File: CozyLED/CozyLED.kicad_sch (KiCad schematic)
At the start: 31 parts, among them J1 BOOT, J3 UART, J4 JTAG, J5 RGB OUT, J6 USB_C_Receptacle_PowerOnly_6P, Q1 Q_NMOS_GDS, Q2 Q_NMOS_GDS, Q3 Q_NMOS_GDS, SW1 SW_Push, U2 LMR16006YQ3, Y1 32.768kHz

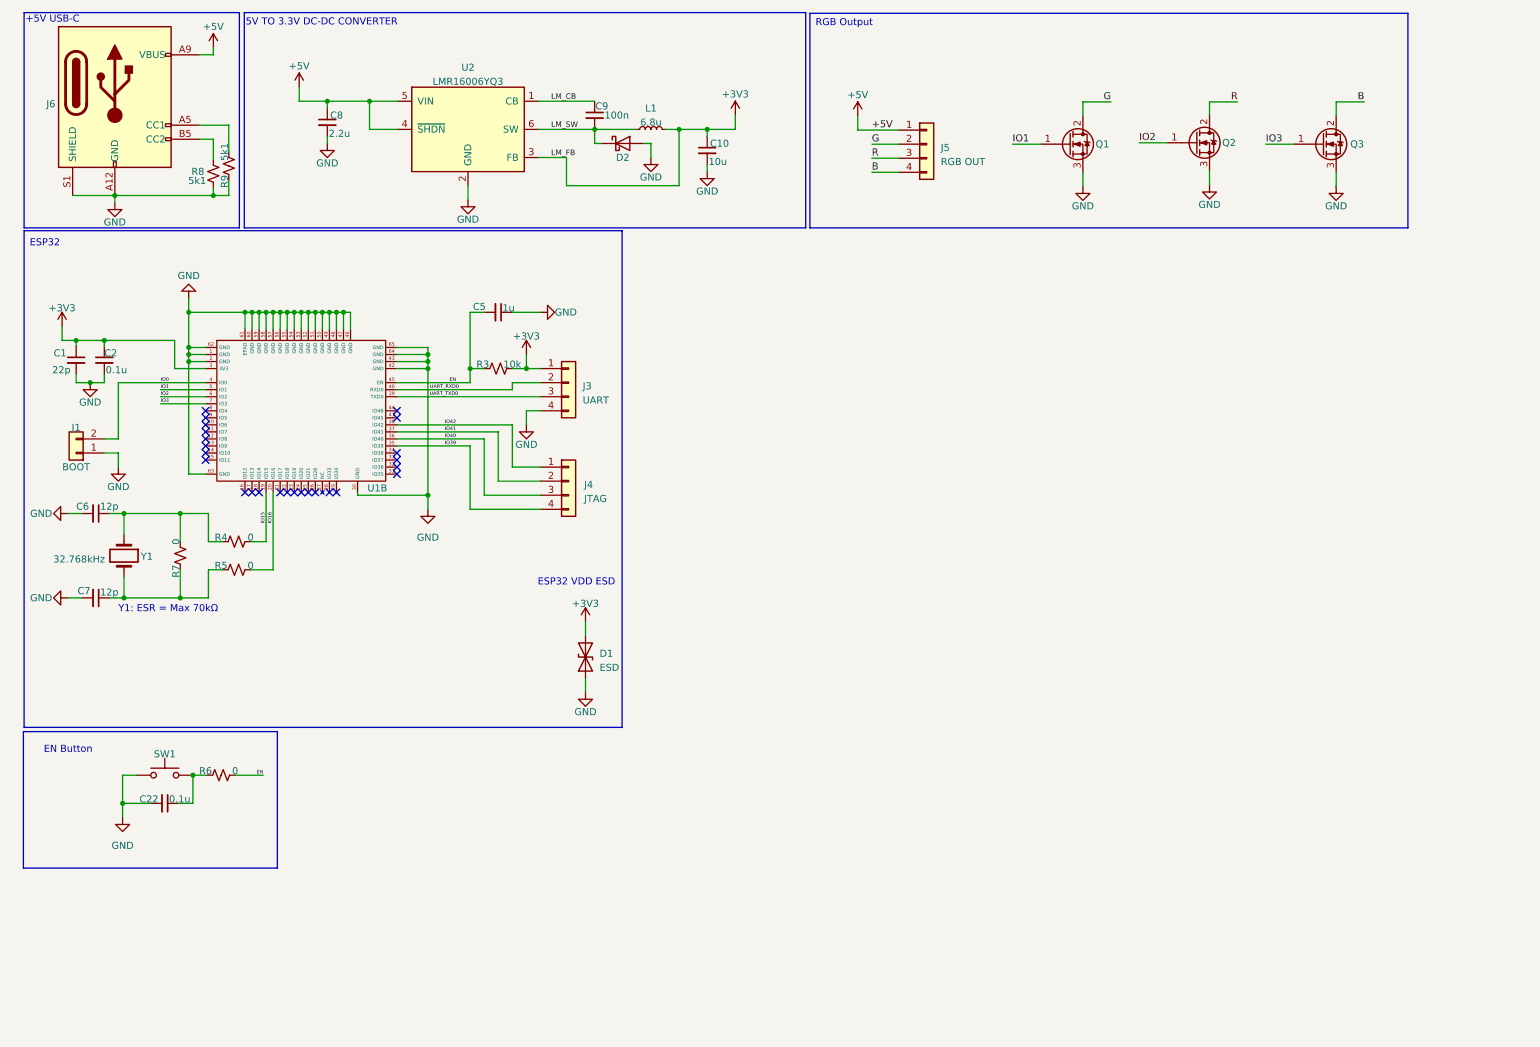
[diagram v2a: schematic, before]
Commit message: Updated Code v0.1
Updates
- Added code for LCD drawings of mode label and triangles to depict button presses (still need actual press drawing)
- Added initial code for mode transition by button hold (2.5 seconds for now)
- Cleaned up some test code
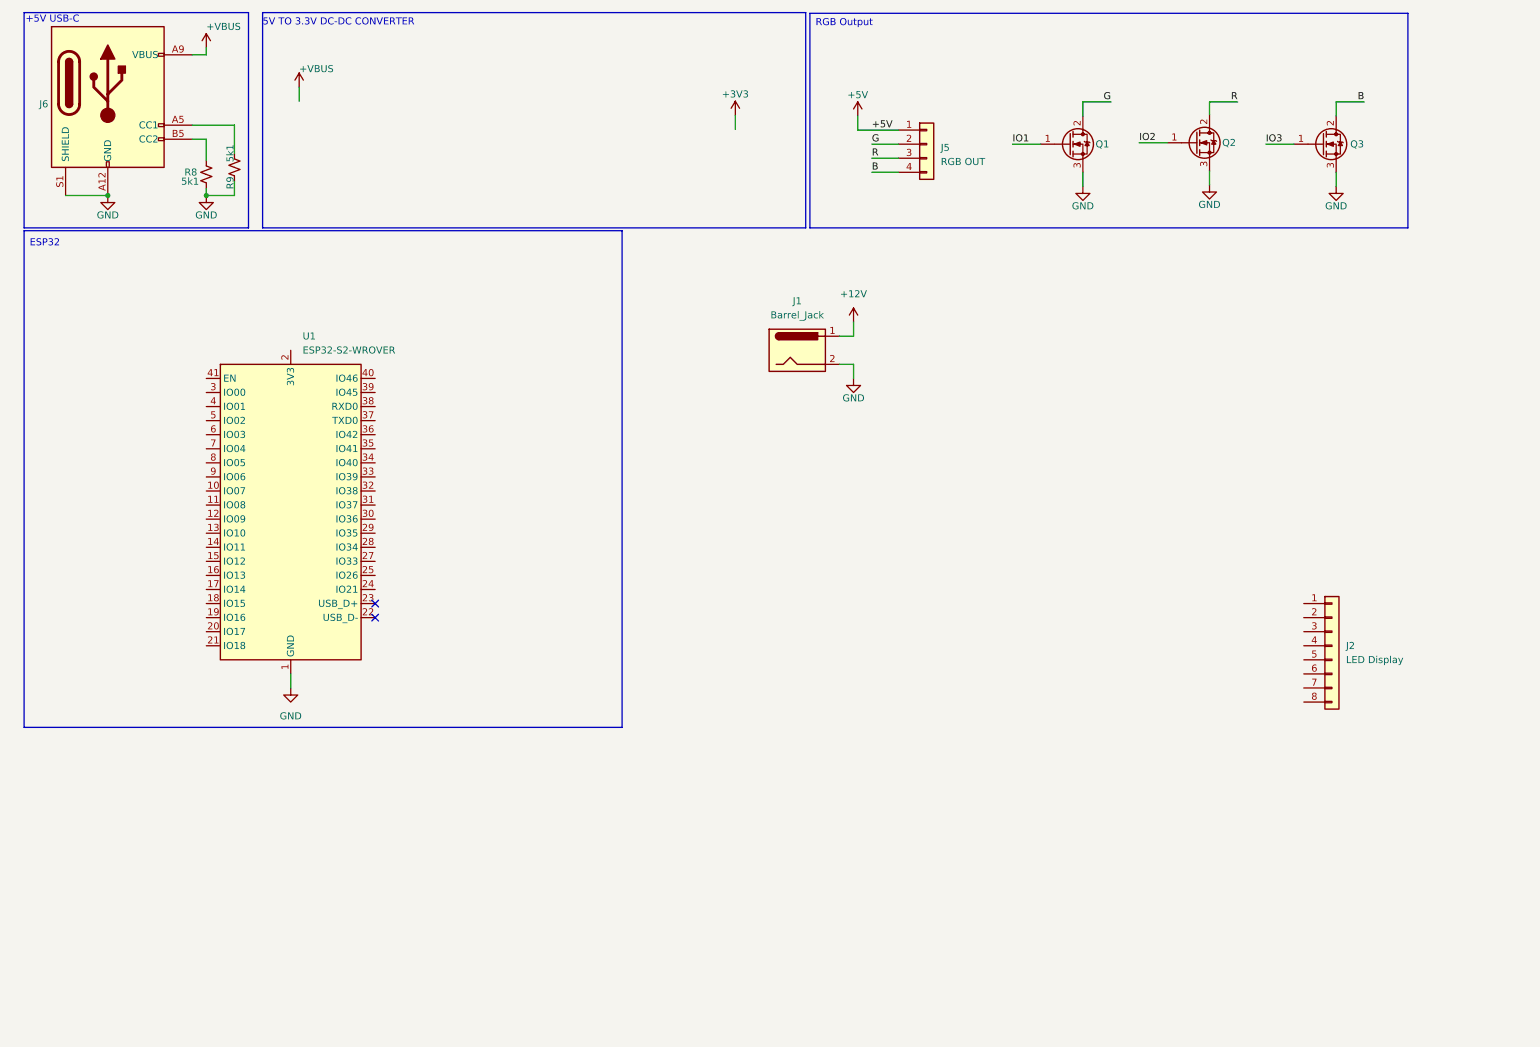
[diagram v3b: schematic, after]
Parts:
- removed C1: 22p, Capacitor_SMD:C_0603_1608Metric, symbol Device:C_Small
- removed C10: 10u, Capacitor_SMD:C_0805_2012Metric, symbol Device:C_Small
- removed C2, C22: 0.1u, Capacitor_SMD:C_0402_1005Metric, symbol Device:C_Small
- removed C5: 1u, Capacitor_SMD:C_0603_1608Metric, symbol Device:C_Small
- removed C6, C7: 12p, Capacitor_SMD:C_0402_1005Metric, symbol Device:C_Small
- removed C8: 2.2u, Capacitor_SMD:C_0603_1608Metric, symbol Device:C_Small
- removed C9: 100n, Capacitor_SMD:C_0402_1005Metric, symbol Device:C_Small
- removed D1: ESD, Diode_SMD:D_SMB, symbol Device:D_TVS
- removed D2: D_Schottky, Diode_SMD:D_0603_1608Metric, symbol Device:D_Schottky
- removed J1: BOOT, Connector_PinHeader_2.00mm:PinHeader_1x02_P2.00mm_Vertical, symbol Connector_Generic:Conn_01x02
- removed J3: UART, Connector_PinHeader_2.00mm:PinHeader_1x04_P2.00mm_Vertical, symbol Connector_Generic:Conn_01x04
- removed J4: JTAG, Connector_PinHeader_2.00mm:PinHeader_1x04_P2.00mm_Vertical, symbol Connector_Generic:Conn_01x04
- removed L1: 6.8u, Inductor_SMD:L_6.3x6.3_H3, symbol Device:L_Small
- removed R3: 10k, Resistor_SMD:R_0402_1005Metric, symbol Device:R_Small_US
- removed R4, R5, R6, R7: 0, Resistor_SMD:R_0402_1005Metric, symbol Device:R_Small_US
- removed SW1: SW_Push, Button_Switch_THT:SW_PUSH_6mm, symbol Switch:SW_Push
- removed U1: ~, ESP32:ESP32_S2_MINI_2, symbol ESP32:ESP32-S2-MINI-2
- removed U2: LMR16006YQ3, Package_TO_SOT_SMD:SOT-23-6, symbol Regulator_Switching:LMR16006YQ3
- removed Y1: 32.768kHz, Crystal:Crystal_SMD_3215-2Pin_3.2x1.5mm, symbol Device:Crystal
- added J1: Barrel_Jack, Connector_BarrelJack:BarrelJack_SwitchcraftConxall_RAPC10U_Horizontal, symbol Connector:Barrel_Jack
- added J2: LED Display, symbol Connector_Generic:Conn_01x08
- added U1: ESP32-S2-WROVER, RF_Module:ESP32-S2-WROVER, symbol RF_Module:ESP32-S2-WROVER
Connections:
- net +5V: no longer J6.A9 (VBUS), J6.B9 (VBUS)
- net GND: now also J1.2, U1.1 (GND), U1.26 (GND), U1.42 (GND), U1.43 (GND)
- new net +12V: J1.1
- new net +VBUS: J6.A9 (VBUS), J6.B9 (VBUS)
- no-connect marks 25 -> 2
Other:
- note removed: "EN Button"
- note removed: "ESP32 VDD ESD"
- note removed: "Y1: ESR = Max 70kΩ"
- moved on the sheet: J6, R8, R9

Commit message: Updated CozyLED schematic
Updates
- Placed initial components of board in  schematic
- Redesigning schematic to not be devboard based but solely ESP32 WROVER-E
- Need to add all the ESP32 components and the DC-DC converter  (12V -> 3V3)
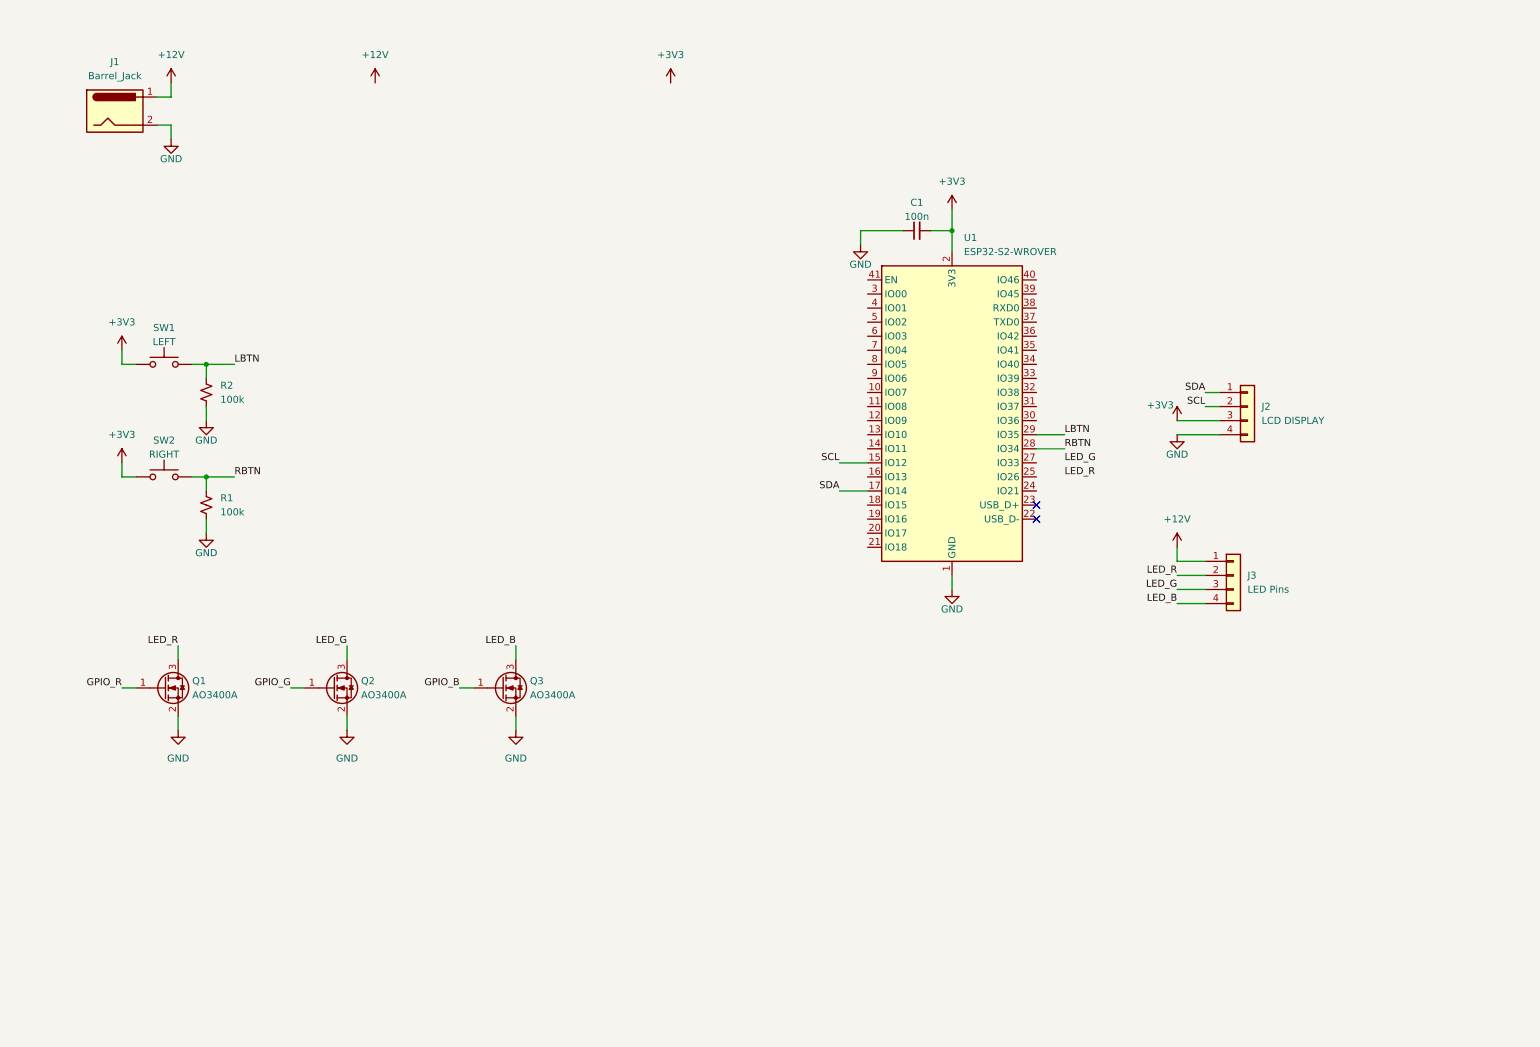
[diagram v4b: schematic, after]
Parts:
- removed J2: LED Display, symbol Connector_Generic:Conn_01x08
- removed J5: RGB OUT, Connector_JST:JST_EH_S4B-EH_1x04_P2.50mm_Horizontal, symbol Connector_Generic:Conn_01x04
- removed J6: USB_C_Receptacle_PowerOnly_6P, Connector_USB:USB_C_Receptacle_GCT_USB4135-GF-A_6P_TopMnt_Horizontal, symbol Connector:USB_C_Receptacle_PowerOnly_6P
- removed Q1, Q2, Q3: Q_NMOS_GDS, Diodes INC:DMN1019USN_N_CHNL, symbol Device:Q_NMOS_GDS
- removed R8, R9: 5k1, Resistor_SMD:R_0402_1005Metric, symbol Device:R_Small_US
- added C1: 100n, symbol Device:C_Small
- added J2: LCD DISPLAY, symbol Connector_Generic:Conn_01x04
- added J3: LED Pins, symbol Connector_Generic:Conn_01x04
- added Q1, Q2, Q3: AO3400A, Package_TO_SOT_SMD:SOT-23, symbol Transistor_FET:AO3400A
- added R1, R2: 100k, symbol Device:R_Small_US
- added SW1: LEFT, symbol Switch:SW_Push
- added SW2: RIGHT, symbol Switch:SW_Push
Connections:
- net +12V: now also J3.1 (Pin_1)
- net +3V3: now also U1.2 (3V3), C1.2, J2.3 (Pin_3), SW1.1, SW2.1
- net GND: now also C1.1, J2.4 (Pin_4), Q1.2 (S), Q2.2 (S), Q3.2 (S), R1.2, R2.2
- net SCL: now reaches U1.15 (IO12)
- net SCL: now also J2.2 (Pin_2)
- net SDA: now reaches U1.17 (IO14)
- net SDA: now also J2.1 (Pin_1)
- net RBTN: now reaches U1.28 (IO34)
- net RBTN: now also R1.1, SW2.2
- net LBTN: now reaches U1.29 (IO35)
- net LBTN: now also R2.1, SW1.2
- new net GPIO_B: Q3.1 (G)
- new net GPIO_G: Q2.1 (G)
- new net GPIO_R: Q1.1 (G)
- new net LED_B: J3.4 (Pin_4), Q3.3 (D)
- new net LED_G: J3.3 (Pin_3), Q2.3 (D)
- new net LED_R: J3.2 (Pin_2), Q1.3 (D)
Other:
- note removed: "+5V USB-C"
- note removed: "5V TO 3.3V DC-DC CONVERTER"
- note removed: "ESP32"
- note removed: "RGB Output"
- moved on the sheet: J1, U1

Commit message: Updated CozyLED PCB
Updates
- Added 12V to 3.3V sw reg (sym+footprint) with its circuitry
- Changed ESP32 symbol to S3 WROVER-E (was incorrectly S2 WROOM) with required circuitry
- Added EN&BOOT buttons
- Added breakout pins for UART, LED, and LCD
- Added nMOS transistors for RGB control (need to change source)
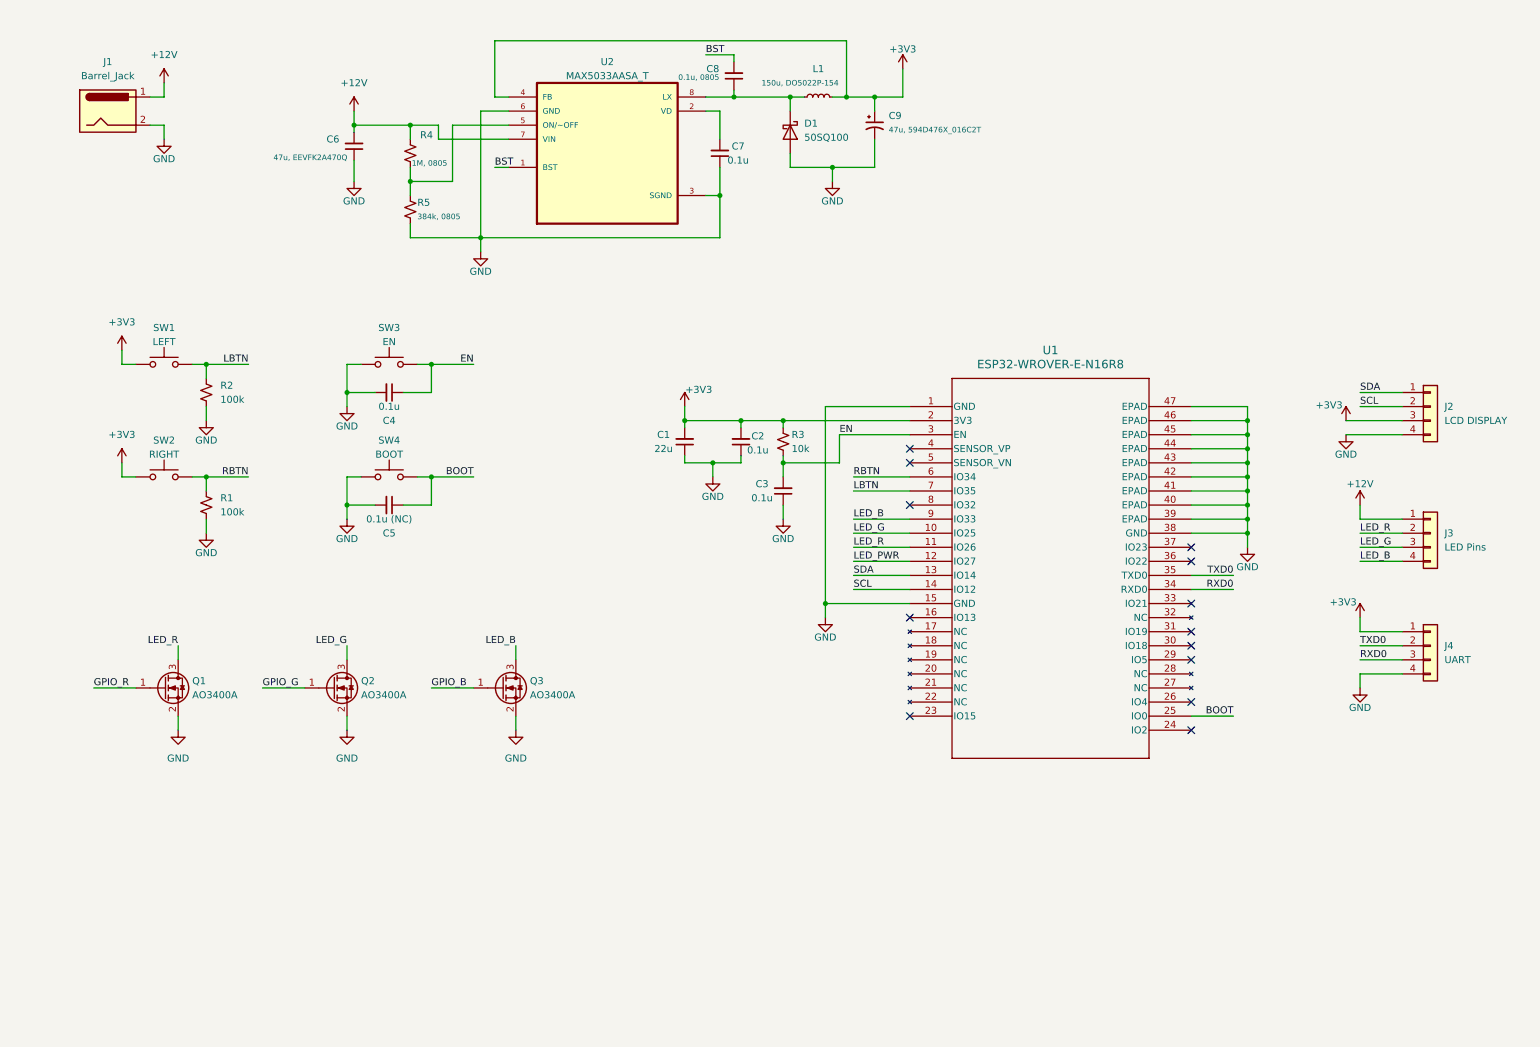
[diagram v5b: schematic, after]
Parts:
- removed U1: ESP32-S2-WROVER, RF_Module:ESP32-S2-WROVER, symbol RF_Module:ESP32-S2-WROVER
- added C2, C3, C4, C7: 0.1u, symbol Device:C_Small
- added C5: 0.1u (NC), symbol Device:C_Small
- added C6: 47u, EEVFK2A470Q, symbol Device:C_Small
- added C8: 0.1u, 0805, symbol Device:C_Small
- added C9: 47u, 594D476X_016C2T, symbol Device:C_Polarized_Small_US
- added D1: 50SQ100, symbol Device:D_Schottky
- added J4: UART, symbol Connector_Generic:Conn_01x04
- added L1: 150u, DO5022P-154, symbol Device:L_Small
- added R3: 10k, symbol Device:R_Small_US
- added R4: 1M, 0805, symbol Device:R_Small_US
- added R5: 384k, 0805, symbol Device:R_Small_US
- added SW3: EN, symbol Switch:SW_Push
- added SW4: BOOT, symbol Switch:SW_Push
- added U1: ESP32-WROVER-E-N16R8, ESP32-WROVER-E_EXP, symbol ESP32:ESP32-WROVER-E-N16R8
- added U2: MAX5033AASA_T, MAX5033AASA_T:SOIC127P600X175-8N, symbol Reg_Switch:MAX5033AASA_T
- C1: value 100n -> 22u
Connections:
- net +12V: now also C6.2, R4.1, U2.7 (VIN)
- net +3V3: now also C2.2, C9.1, J4.1 (Pin_1), L1.2, R3.1, U1.2 (3V3), U2.4 (FB)
- net GND: now also C2.1, C3.1, C4.2, C5.2, C6.1, C7.1, C9.2, D1.2 (A), J4.4 (Pin_4), R5.2, SW3.1, SW4.1, U1.1 (GND), U1.15 (GND), U1.38 (GND), U1.39 (EPAD), U1.40 (EPAD), U1.41 (EPAD), U1.42 (EPAD), U1.43 (EPAD), U1.44 (EPAD), U1.45 (EPAD), U1.46 (EPAD), U1.47 (EPAD), U2.3 (SGND), U2.6 (GND)
- net LBTN: now also U1.7 (IO35)
- net LED_B: now also U1.9 (IO33)
- net LED_G: now also U1.10 (IO25)
- net LED_R: now also U1.11 (IO26)
- net RBTN: now also U1.6 (IO34)
- net SCL: now also U1.14 (IO12)
- net SDA: now also U1.13 (IO14)
- new net: R4.2, R5.1, U2.5 (ON/~OFF)
- new net: C8.1, D1.1 (K), L1.1, U2.8 (LX)
- new net: C7.2, U2.2 (VD)
- new net BOOT: C5.1, SW4.2, U1.25 (IO0)
- new net BST: C8.2, U2.1 (BST)
- new net EN: C3.2, C4.1, R3.2, SW3.2, U1.3 (EN)
- new net LED_PWR: U1.12 (IO27)
- new net RXD0: J4.3 (Pin_3), U1.34 (RXD0)
- new net TXD0: J4.2 (Pin_2), U1.35 (TXD0)
- no-connect marks 2 -> 13
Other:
- moved on the sheet: C1, J1, J2, J3
